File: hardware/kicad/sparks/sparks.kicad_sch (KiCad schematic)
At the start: 0 parts

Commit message: Add TP4056 and CC1101 libraries, start the schematic
Vendor the TP4056 breakout symbol and footprint, and a CC1101
module symbol converted from the legacy KiCad 5 .lib format.
Neither part is in the KiCad stock libraries.

Do not vendor the upstream CC1101 footprint: it is a single
column of 8 pads at 2.0 mm pitch, belonging to a bare
Homematic-style board. The module used here has 8 pins in two
rows of four at 2.54 mm, so a stock PinHeader_2x04_P2.54mm
footprint is correct instead.

Flag the TP4056 footprint as unverified. Its pad spacing is
irregular rather than on a 2.54 mm grid, so it is specific to
one board revision and may not fit a module from another
seller. Measure before committing the PCB to the laser.

Place the first three schematic symbols: the ESP32-C3
SuperMini, the MAX7219 and the TP4056 breakout.

Register the local libraries with ${KIPRJMOD}-relative paths so
the project resolves them on any machine, rather than the
absolute paths KiCad writes by default.
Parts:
- added J1: TP4056 Breakout, TP4056_breakout:TP4056_breakout, symbol TP4056-Breakout:TP4056_breakout
- added U1: MAX7219, symbol Driver_LED:MAX7219
- added U2: ESP32-C3-SuperMini, ESP32-C3-SuperMini:ESP32-C3-SuperMini, symbol ESP32-C3-SuperMini:ESP32-C3-SuperMini
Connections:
- new net: U1.4 (GND), U1.9 (GND)

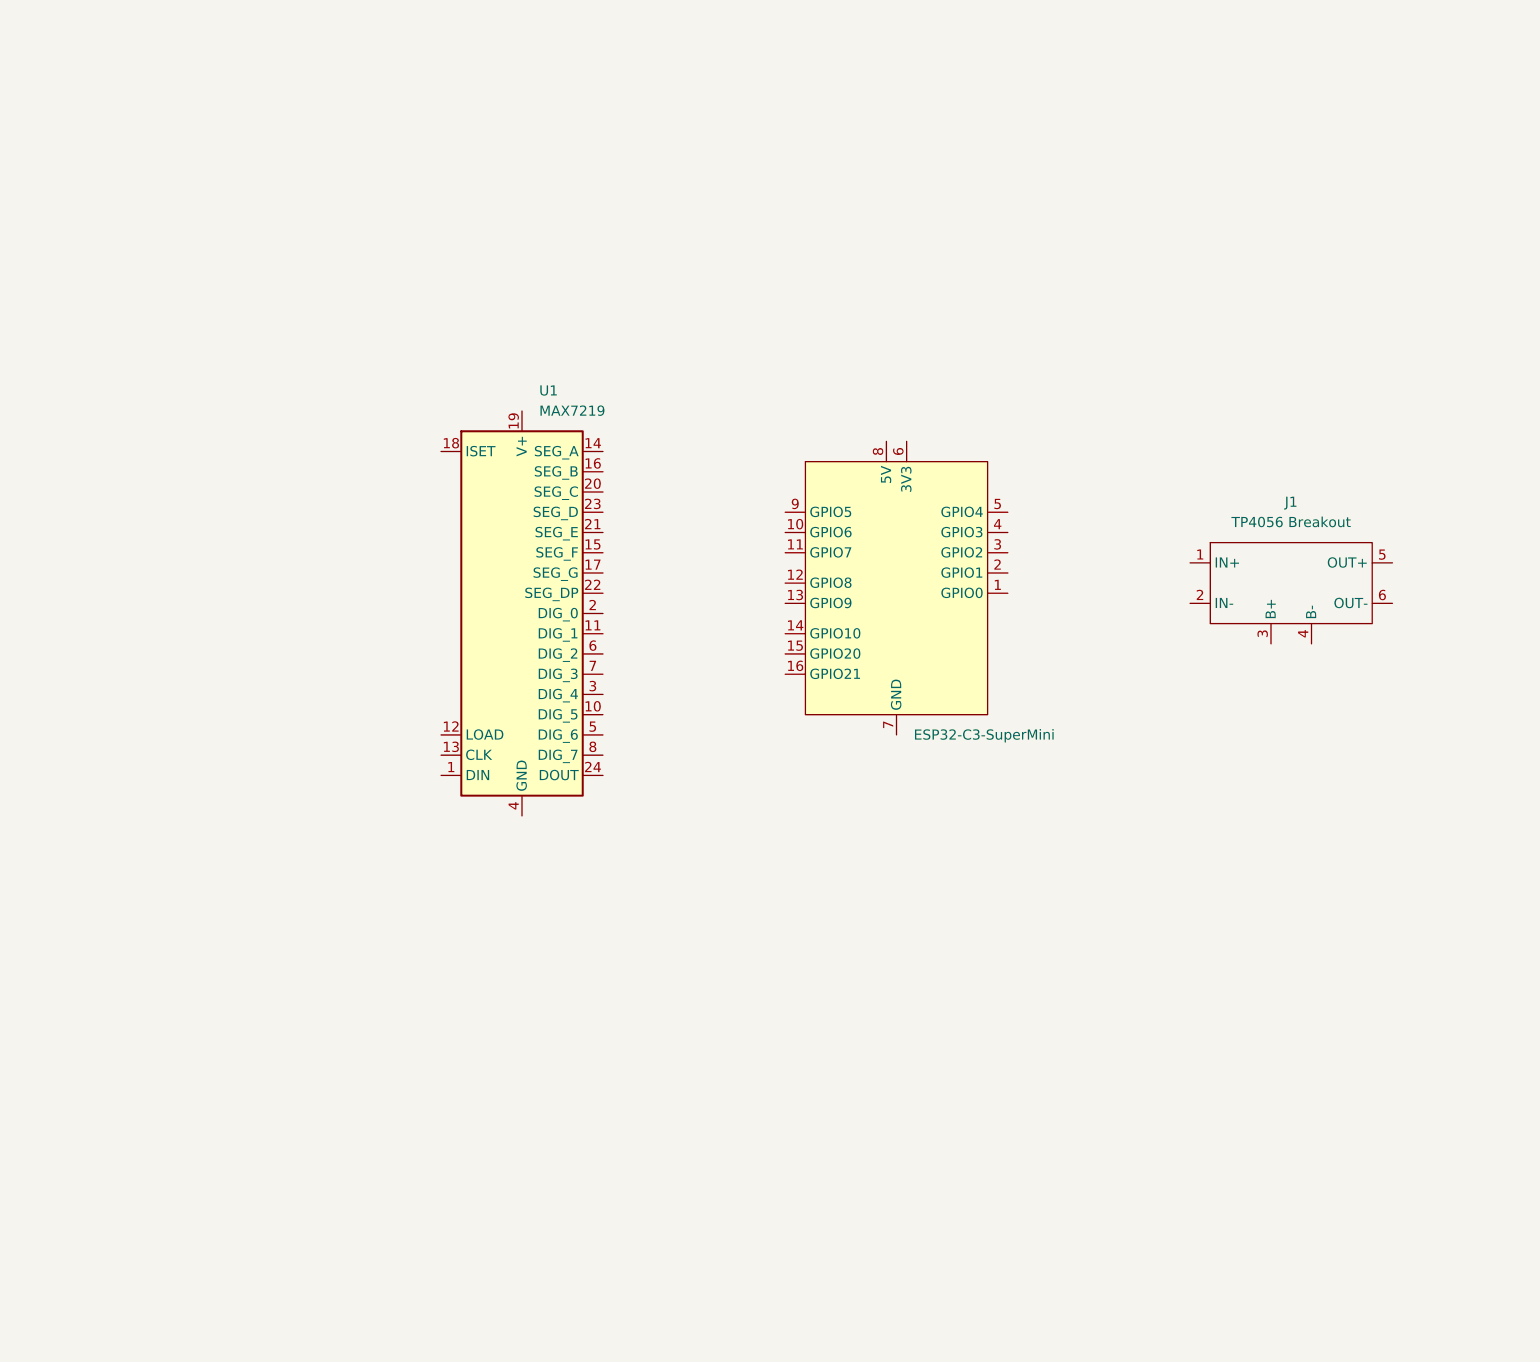
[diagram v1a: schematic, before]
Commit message: Complete the schematic
Wire the full circuit: the 26-LED matrix, the MAX7219 driver, the
ESP32-C3, the CC1101 socket, the TP4056 charger and the battery
sense divider. ERC passes with no errors.

The LED matrix is verified against the Morse tree by exporting the
netlist and checking every diode: all 26 sit on the SEG/DIG pair
their letter's code requires, including the gaps at SEG3 and SEG5
in the DIG3 row where the non-English letters would be.

Set the battery divider to 220k/220k, halving cell voltage into the
ADC range for about 9.5 uA of drain.

Choose the remaining parts: a 12 mm magnetic buzzer, a 6 mm tactile
switch, and a 102050 1000 mAh LiPo pouch giving roughly seven hours
in trainer mode. Assign footprints to all 40 components.

Drop the CC1101 symbol. The board carries only an 8-pin socket, so
a generic Conn_02x04_Odd_Even describes it accurately and the module
plugs in only when the radio is used.

Register the local footprint libraries in fp-lib-table. They had
been added to design-block-lib-table, which is a different feature
and left the footprints unfindable. Also rename the TP4056
footprint's internal name to match its filename, since KiCad
resolves footprints by the internal name.
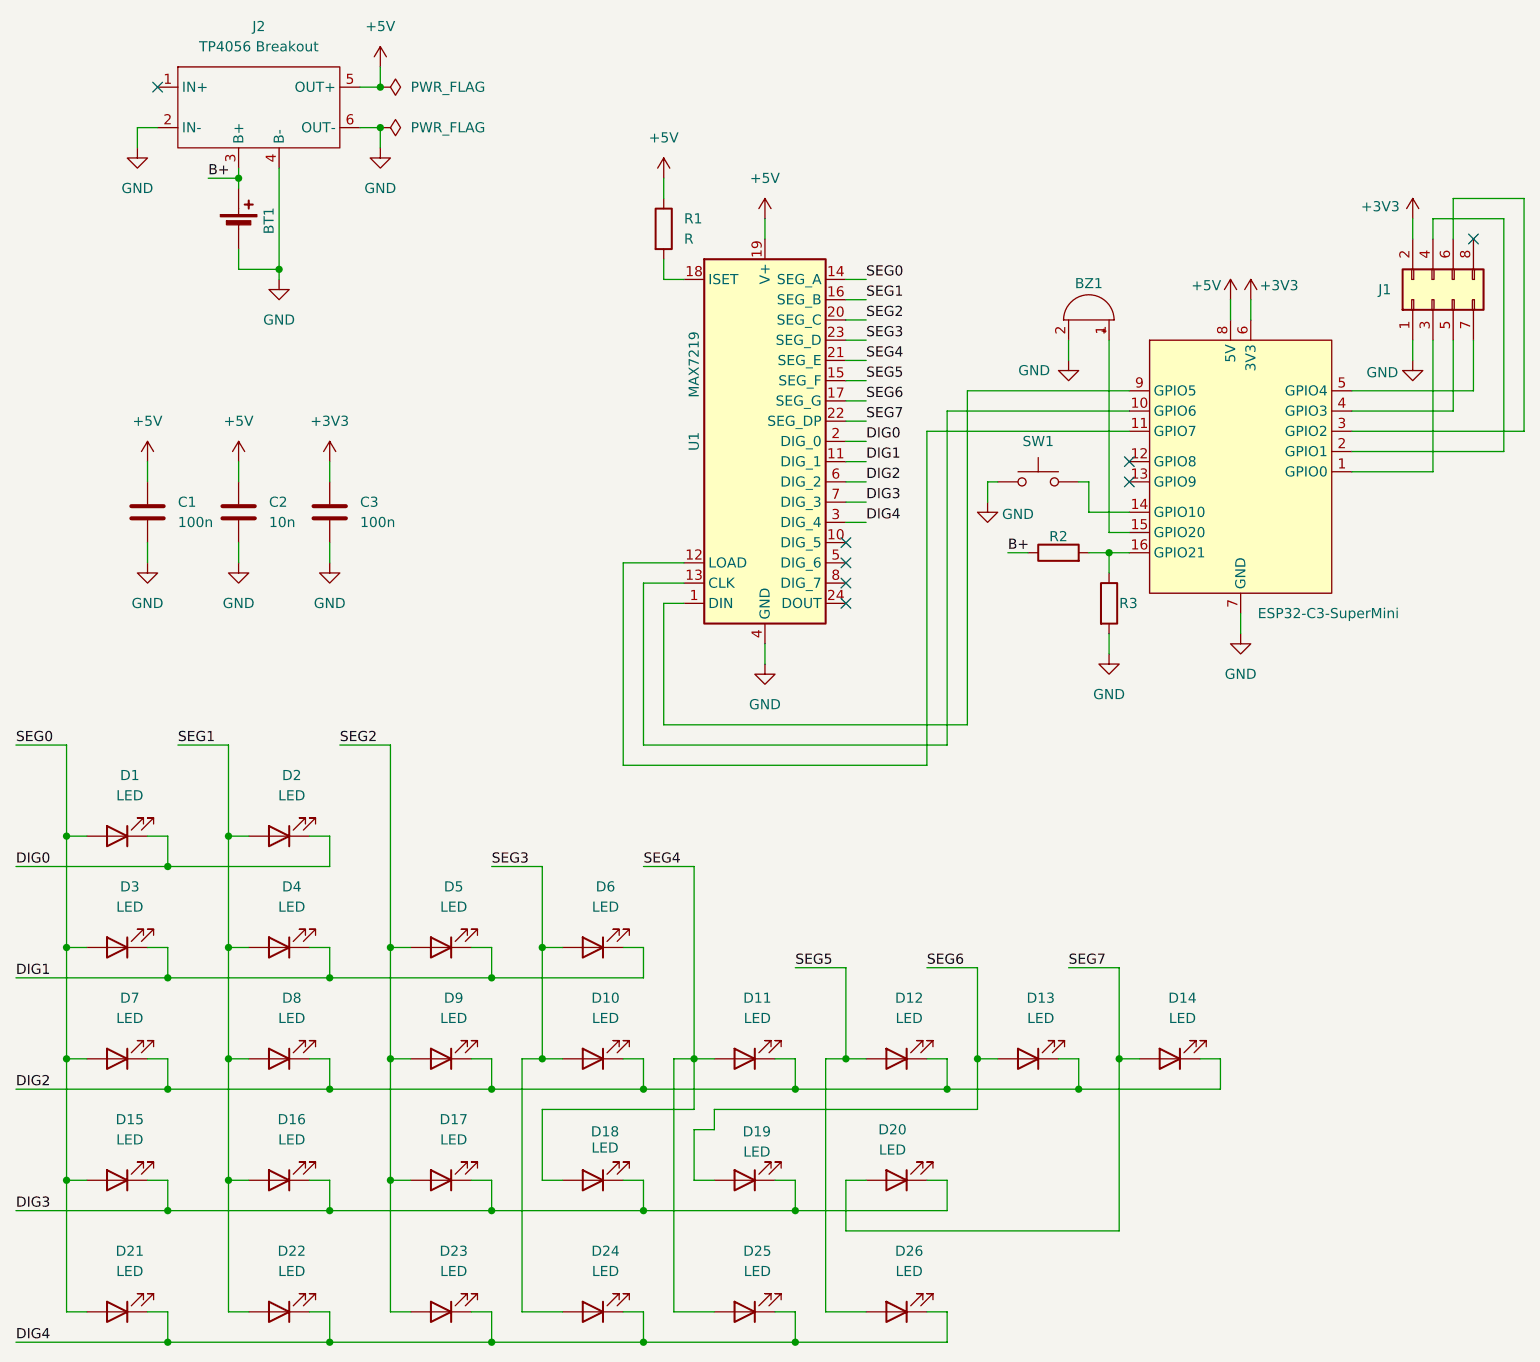
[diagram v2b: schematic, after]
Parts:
- added BT1: Battery_Cell, Connector_Wire:SolderWire-0.127sqmm_1x02_P3.7mm_D0.48mm_OD1mm_Relief, symbol Device:Battery_Cell
- added BZ1: Buzzer, Buzzer_Beeper:Buzzer_12x9.5RM7.6, symbol Device:Buzzer
- added C1, C3: 100n, Capacitor_SMD:C_0805_2012Metric_Pad1.18x1.45mm_HandSolder, symbol Device:C
- added C2: 10n, Capacitor_SMD:C_0805_2012Metric_Pad1.18x1.45mm_HandSolder, symbol Device:C
- added D1, D10, D11, D12, D13, D14, D15, D16, D17, D18, D19, D2, D20, D21, D22, D23, D24, D25, D26, D3, D4, D5, D6, D7, D8, D9: LED, LED_SMD:LED_0805_2012Metric_Pad1.15x1.40mm_HandSolder, symbol Device:LED
- added J1: Conn_02x04_Odd_Even, Connector_PinSocket_2.54mm:PinSocket_2x04_P2.54mm_Vertical, symbol Connector_Generic:Conn_02x04_Odd_Even
- added R1: R, Resistor_SMD:R_0805_2012Metric_Pad1.20x1.40mm_HandSolder, symbol Device:R
- added R2, R3: 220k, Resistor_SMD:R_0805_2012Metric_Pad1.20x1.40mm_HandSolder, symbol Device:R
- added SW1: SW_Push, Button_Switch_THT:SW_PUSH_6mm, symbol Switch:SW_Push
- J2: renamed from J1; footprint TP4056_breakout:TP4056_breakout -> TP4056-Breakout:TP4056-Breakout
- U1: footprint (none) -> Package_DIP:DIP-24_W7.62mm
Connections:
- net at U2.1 (GPIO0): now also J1.3 (Pin_3)
- net at U2.10 (GPIO6): now also U1.13 (CLK)
- net at U2.11 (GPIO7): now also U1.12 (LOAD)
- net at U2.14 (GPIO10): now also SW1.2
- net at U2.15 (GPIO20): now also BZ1.1 (+)
- net at U2.16 (GPIO21): now also R2.2, R3.1
- net at U2.2 (GPIO1): now also J1.4 (Pin_4)
- net at U2.3 (GPIO2): now also J1.6 (Pin_6)
- net at U2.4 (GPIO3): now also J1.5 (Pin_5)
- net at U2.5 (GPIO4): now also J1.7 (Pin_7)
- net +3V3: now reaches U2.6 (3V3)
- net +3V3: now also C3.1, J1.2 (Pin_2)
- net GND: now reaches U2.7 (GND)
- net GND: now also J2.2 (IN-), J2.4 (B-), J2.6 (OUT-), U1.4 (GND), U1.9 (GND), BT1.2 (-), BZ1.2 (-), C1.2, C2.2, C3.2, J1.1 (Pin_1), R3.2, SW1.1
- net +5V: now reaches U2.8 (5V)
- net +5V: now also J2.5 (OUT+), U1.19 (V+), C1.1, C2.1, R1.1
- net at U2.9 (GPIO5): now also U1.1 (DIN)
- net DIG1: now reaches U1.11 (DIG_1)
- net DIG1: now also D3.1 (K), D4.1 (K), D5.1 (K), D6.1 (K)
- net SEG0: now reaches U1.14 (SEG_A)
- net SEG0: now also D1.2 (A), D15.2 (A), D21.2 (A), D3.2 (A), D7.2 (A)
- net SEG5: now reaches U1.15 (SEG_F)
- net SEG5: now also D12.2 (A), D26.2 (A)
- net SEG1: now reaches U1.16 (SEG_B)
- net SEG1: now also D16.2 (A), D2.2 (A), D22.2 (A), D4.2 (A), D8.2 (A)
- net SEG6: now reaches U1.17 (SEG_G)
- net SEG6: now also D13.2 (A), D19.2 (A)
- net at U1.18 (ISET): now also R1.2
- net DIG0: now reaches U1.2 (DIG_0)
- net DIG0: now also D1.1 (K), D2.1 (K)
- net SEG2: now reaches U1.20 (SEG_C)
- net SEG2: now also D17.2 (A), D23.2 (A), D5.2 (A), D9.2 (A)
- net SEG4: now reaches U1.21 (SEG_E)
- net SEG4: now also D11.2 (A), D18.2 (A), D25.2 (A)
- net SEG7: now reaches U1.22 (SEG_DP)
- net SEG7: now also D14.2 (A), D20.2 (A)
- net SEG3: now reaches U1.23 (SEG_D)
- net SEG3: now also D10.2 (A), D24.2 (A), D6.2 (A)
- net DIG4: now reaches U1.3 (DIG_4)
- net DIG4: now also D21.1 (K), D22.1 (K), D23.1 (K), D24.1 (K), D25.1 (K), D26.1 (K)
- net DIG2: now reaches U1.6 (DIG_2)
- net DIG2: now also D10.1 (K), D11.1 (K), D12.1 (K), D13.1 (K), D14.1 (K), D7.1 (K), D8.1 (K), D9.1 (K)
- net DIG3: now reaches U1.7 (DIG_3)
- net DIG3: now also D15.1 (K), D16.1 (K), D17.1 (K), D18.1 (K), D19.1 (K), D20.1 (K)
- net B+: now reaches J2.3 (B+)
- net B+: now also BT1.1 (+), R2.1
- no-connect marks 0 -> 8
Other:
- moved on the sheet: J2, U1

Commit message: Switch to the HW-357 combined charger and boost module
Power now comes from an HW-357: a TP4056 charger and an MT3608
boost converter on one board with its own micro-USB socket. Its
IN+/IN- pads are left unconnected, since charging goes through
that socket.

This resolves the open supply question. The +5V net carries a
genuine regulated 5 V instead of raw cell voltage, so the MAX7219
keeps proper headroom above the white LEDs' ~3.4 V forward drop
and the panel no longer dims as the battery drains.

Record the cost: a boost draws more current than it supplies, so
delivering 139 mA at 5 V pulls about 190 mA from the cell and the
1000 mAh pack gives roughly five hours rather than seven.

Warn that the MT3608 trimmer is uncalibrated on arrival. It must
be set to 5.0 V in isolation before the module is connected to
anything, or it will destroy the ESP32-C3 and the MAX7219.
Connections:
- net GND: no longer J2.2 (IN-)
- no-connect marks 8 -> 9
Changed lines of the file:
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@@
 	)
 	(no_connect
+		(at 36.83 38.1)
+	)
+	(no_connect
 		(at 201.93 52.07)
 	)
@@
 	(wire
 		(pts
-			(xy 36.83 38.1) (xy 34.29 38.1)
-		)
-		(stroke
-			(width 0)
-			(type default)
-		)
-	)
-	(wire
-		(pts
 			(xy 100.33 113.03) (xy 138.43 113.03)
 		)
@@
 	(wire
 		(pts
-			(xy 34.29 38.1) (xy 34.29 40.64)
-		)
-		(stroke
-			(width 0)
-			(type default)
-		)
-	)
-	(wire
-		(pts
 			(xy 58.42 80.01) (xy 58.42 82.55)
 		)
@@
 					(unit 1)
 				)
-			)
-		)
-	)
-	(symbol
-		(lib_id "power:GND")
-		(at 34.29 40.64 0)
-		(unit 1)
-		(body_style 1)
-		(exclude_from_sim no)
-		(in_bom yes)
-		(on_board yes)
-		(in_pos_files yes)
-		(dnp no)
-		(fields_autoplaced yes)
-		(property "Reference" "#PWR010"
-			(at 34.29 46.99 0)
-			(hide yes)
-			(show_name no)
-			(do_not_autoplace no)
-			(effects
-				(font
-					(size 1.27 1.27)
-				)
-			)
-		)
-		(property "Value" "GND"
-			(at 34.29 45.72 0)
-			(show_name no)
-			(do_not_autoplace no)
-			(effects
-				(font
-					(size 1.27 1.27)
-				)
-			)
-		)
-		(property "Footprint" ""
-			(at 34.29 40.64 0)
-			(hide yes)
-			(show_name no)
-			(do_not_autoplace no)
-			(effects
-				(font
-					(size 1.27 1.27)
-				)
-			)
-		)
-		(property "Datasheet" ""
-			(at 34.29 40.64 0)
-			(hide yes)
-			(show_name no)
-			(do_not_autoplace no)
-			(effects
-				(font
-					(size 1.27 1.27)
-				)
-			)
-		)
-		(property "Description" "Power symbol creates a global label with name \"GND\" , ground"
-			(at 34.29 40.64 0)
-			(hide yes)
-			(show_name no)
-			(do_not_autoplace no)
-			(effects
-				(font
-					(size 1.27 1.27)
-				)
-			)
-		)
-		(pin "1"
-		)
-		(instances
-			(project "sparks"
-				(path "/b32579de-9b7d-4099-823e-c649101f67ab"
-					(reference "#PWR010")
-					(unit 1)
-				)

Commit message: Add a CC1101 socket footprint with the module's own pin numbering
The stock PinSocket_2x04 numbers pads 2/1, 4/3, 6/5, 8/7 across the
two rows, which put pin 1 on the outward-facing row. The module has
pin 1 (GND) on the row nearest the board and pin 2 (3V3) on the
outward row.

No rotation of the stock footprint produces that arrangement: 90 and
270 turn it sideways into two columns of four, and 180 swaps the
columns as well as the rows. It needs a mirror, which a footprint
cannot do without changing layers.

Add Sparks:CC1101_Socket_2x04 with pad positions written explicitly
so that at rotation 0 the top row is 2 4 6 8 and the bottom row,
against the board, is 1 3 5 7.

Register the Sparks.pretty library in fp-lib-table.
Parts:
- J1: footprint Connector_PinSocket_2.54mm:PinSocket_2x04_P2.54mm_Vertical -> Sparks:CC1101_Socket_2x04
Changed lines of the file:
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@@
 			)
 		)
-		(property "Footprint" "Connector_PinSocket_2.54mm:PinSocket_2x04_P2.54mm_Vertical"
+		(property "Footprint" "Sparks:CC1101_Socket_2x04"
 			(at 196.85 59.69 0)
 			(hide yes)
